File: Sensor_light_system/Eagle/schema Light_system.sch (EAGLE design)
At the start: 4 parts

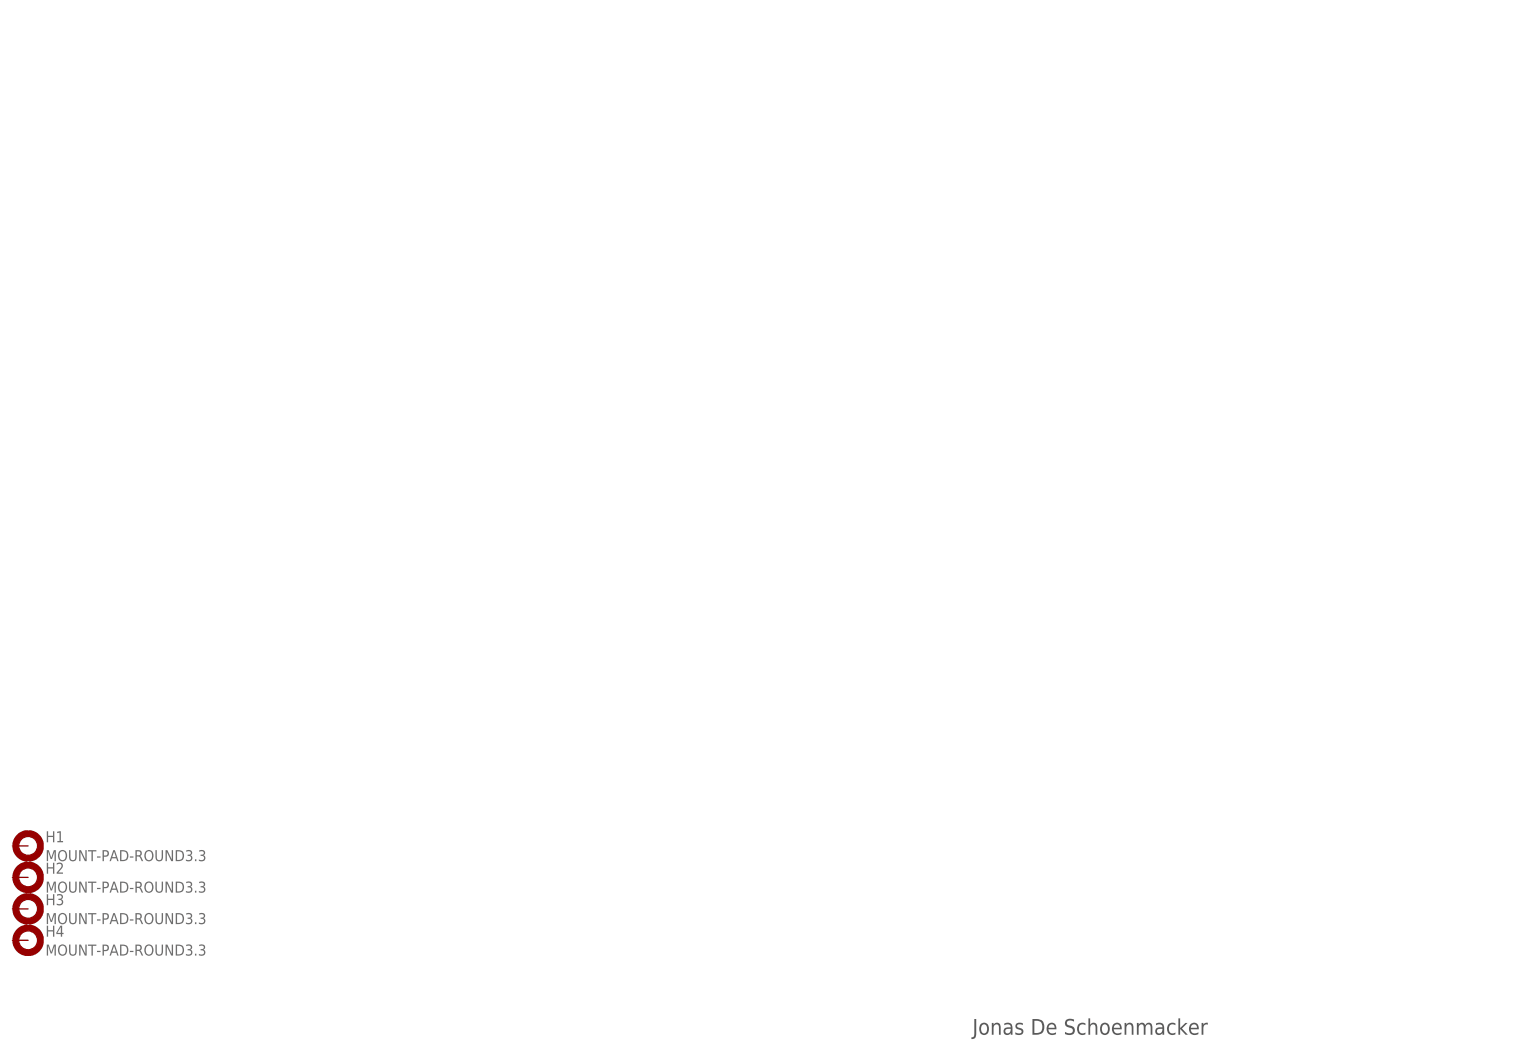
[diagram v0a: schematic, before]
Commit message: schema sensor aangepast
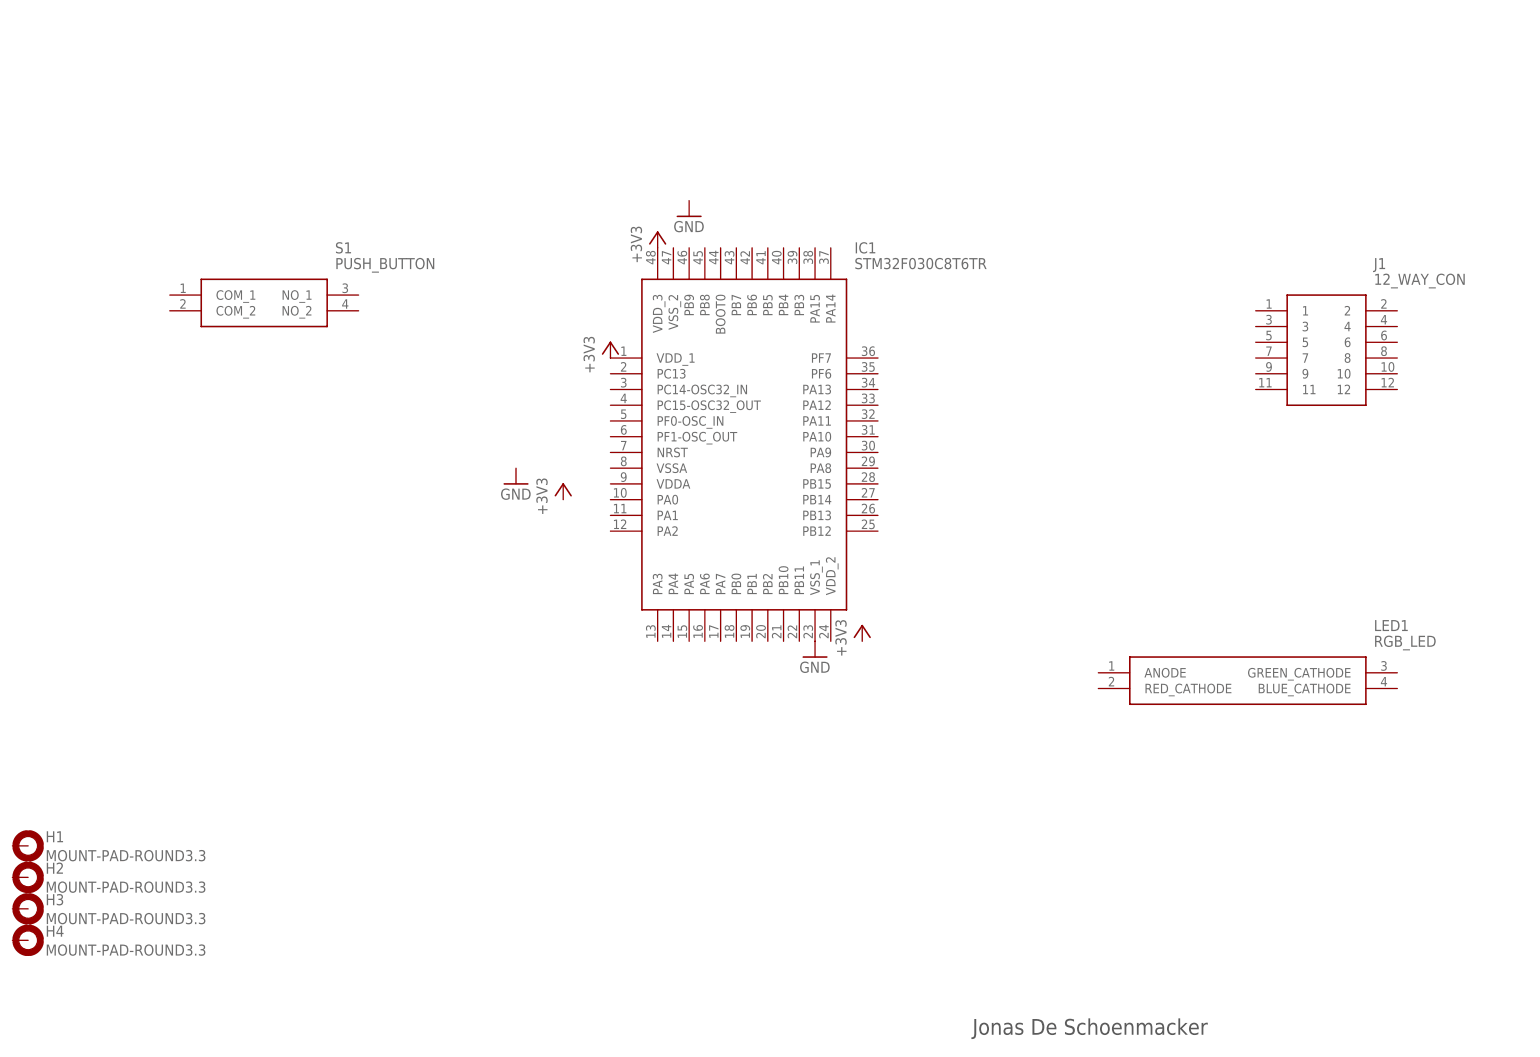
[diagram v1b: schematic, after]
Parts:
- added IC1: STM32F030C8T6TR, Library light system:STM32F030C8T6TR
- added J1: 12_WAY_CON, Library light system:12_WAY_CON
- added LED1: RGB_LED, Library light system:RGB_LED
- added S1: PUSH_BUTTON, Library light system:PUSH_BUTTON
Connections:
- new net +3V3: IC1.VDD_1, IC1.VDD_3
- new net GND: IC1.VSS_1, S1.P, S1.P1
- new net N$6: S1.S, S1.S1
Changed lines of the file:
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@@
 <part name="H3" library="holes" library_urn="urn:adsk.eagle:library:237" deviceset="MOUNT-PAD-ROUND" device="3.3" package3d_urn="urn:adsk.eagle:package:14283/1"/>
 <part name="H4" library="holes" library_urn="urn:adsk.eagle:library:237" deviceset="MOUNT-PAD-ROUND" device="3.3" package3d_urn="urn:adsk.eagle:package:14283/1"/>
+<part name="IC1" library="Library light system" deviceset="STM32F030C8T6TR" device=""/>
+<part name="LED1" library="Library light system" deviceset="RGB_LED" device=""/>
+<part name="S1" library="Library light system" deviceset="PUSH_BUTTON" device=""/>
+<part name="J1" library="Library light system" deviceset="12_WAY_CON" device=""/>
+<part name="+3V1" library="supply1" library_urn="urn:adsk.eagle:library:371" deviceset="+3V3" device=""/>
+<part name="+3V2" library="supply1" library_urn="urn:adsk.eagle:library:371" deviceset="+3V3" device=""/>
+<part name="+3V3" library="supply1" library_urn="urn:adsk.eagle:library:371" deviceset="+3V3" device=""/>
+<part name="GND1" library="supply1" library_urn="urn:adsk.eagle:library:371" deviceset="GND" device=""/>
+<part name="GND2" library="supply1" library_urn="urn:adsk.eagle:library:371" deviceset="GND" device=""/>
+<part name="GND3" library="supply1" library_urn="urn:adsk.eagle:library:371" deviceset="GND" device=""/>
+<part name="+3V4" library="supply1" library_urn="urn:adsk.eagle:library:371" deviceset="+3V3" device=""/>
 </parts>
 <sheets>
@@
 <attribute name="VALUE" x="15.494" y="20.3962" size="1.778" layer="96"/>
 </instance>
+<instance part="IC1" gate="G$1" x="106.68" y="116.84">
+<attribute name="NAME" x="146.05" y="134.62" size="1.778" layer="95" align="center-left"/>
+<attribute name="VALUE" x="146.05" y="132.08" size="1.778" layer="96" align="center-left"/>
+</instance>
+<instance part="LED1" gate="G$1" x="185.42" y="66.04">
+<attribute name="NAME" x="229.87" y="73.66" size="1.778" layer="95" align="center-left"/>
+<attribute name="VALUE" x="229.87" y="71.12" size="1.778" layer="96" align="center-left"/>
+</instance>
+<instance part="S1" gate="G$1" x="35.56" y="127">
+<attribute name="NAME" x="62.23" y="134.62" size="1.778" layer="95" align="center-left"/>
+<attribute name="VALUE" x="62.23" y="132.08" size="1.778" layer="96" align="center-left"/>
+</instance>
+<instance part="J1" gate="G$1" x="210.82" y="124.46">
+<attribute name="NAME" x="229.87" y="132.08" size="1.778" layer="95" align="center-left"/>
+<attribute name="VALUE" x="229.87" y="129.54" size="1.778" layer="96" align="center-left"/>
+</instance>
+<instance part="+3V1" gate="G$1" x="106.68" y="119.38">
+<attribute name="VALUE" x="104.14" y="114.3" size="1.778" layer="96" rot="R90"/>
+</instance>
+<instance part="+3V2" gate="G$1" x="147.32" y="73.66">
+<attribute name="VALUE" x="144.78" y="68.58" size="1.778" layer="96" rot="R90"/>
+</instance>
+<instance part="+3V3" gate="G$1" x="114.3" y="137.16">
+<attribute name="VALUE" x="111.76" y="132.08" size="1.778" layer="96" rot="R90"/>
+</instance>
+<instance part="GND1" gate="1" x="139.7" y="68.58">
+<attribute name="VALUE" x="137.16" y="66.04" size="1.778" layer="96"/>
+</instance>
+<instance part="GND2" gate="1" x="91.44" y="96.52">
+<attribute name="VALUE" x="88.9" y="93.98" size="1.778" layer="96"/>
+</instance>
+<instance part="GND3" gate="1" x="119.38" y="139.7">
+<attribute name="VALUE" x="116.84" y="137.16" size="1.778" layer="96"/>
+</instance>
+<instance part="+3V4" gate="G$1" x="99.06" y="96.52">
+<attribute name="VALUE" x="96.52" y="91.44" size="1.778" layer="96" rot="R90"/>
+</instance>
 </instances>
 <busses>
 </busses>
 <nets>
+<net name="+3V3" class="0">
+<segment>
+<pinref part="IC1" gate="G$1" pin="VDD_1"/>
+<pinref part="+3V1" gate="G$1" pin="+3V3"/>
+</segment>
+<segment>
+<pinref part="IC1" gate="G$1" pin="VDD_3"/>
+<pinref part="+3V3" gate="G$1" pin="+3V3"/>
+</segment>
+</net>
+<net name="GND" class="0">
+<segment>
+<pinref part="IC1" gate="G$1" pin="VSS_1"/>
+<pinref part="GND1" gate="1" pin="GND"/>
+</segment>
+</net>
 </nets>
 </sheet>

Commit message: schema sensoren
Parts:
- added JP1, JP2, JP3: (no value), jumper:JP4Q
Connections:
- new net N$1: JP1.2
- new net N$3: IC1.NRST, JP3.2, S1.NO_1, S1.NO_2
- new net N$5: JP2.2
- new net N$9: JP1.3, JP1.4
- net +3V3: now also IC1.VDDA, IC1.VDD_2, JP1.1, JP2.1, JP3.1
- net GND: now also IC1.VSSA, IC1.VSS_2, JP1.5, JP2.3, JP3.3, S1.COM_1, S1.COM_2
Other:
- moved on the sheet: S1
